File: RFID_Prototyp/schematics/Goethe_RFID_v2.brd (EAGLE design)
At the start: 57.1 x 53.3 mm, 61 parts, among them IC2 LM2937, M1 ARDUINO_R3_SMALL, Q1 IRF8313P, Q2 IRF8313P, Q3 IRF8313P, X1 12V supply

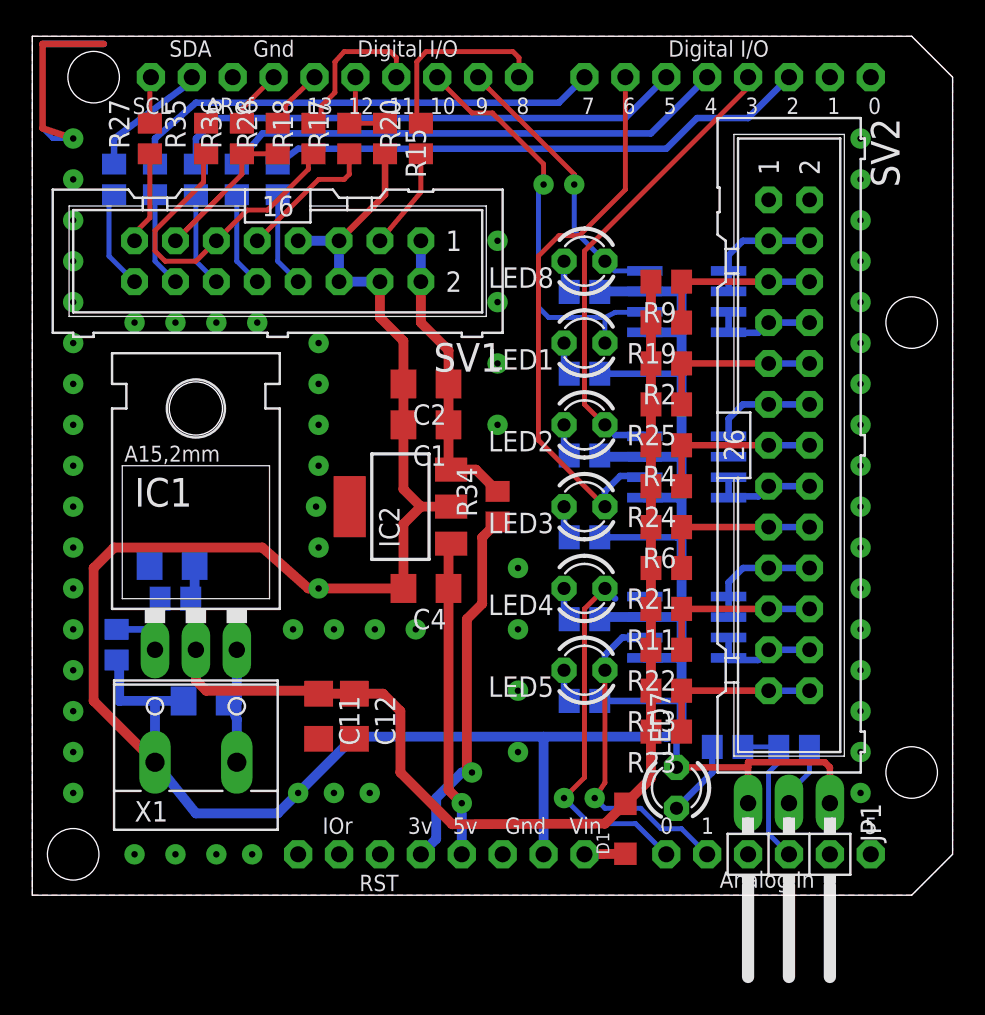
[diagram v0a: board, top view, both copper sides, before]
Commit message: Add RFID lib to repo; Adjust LED regulator voltage; Split RFID firmware in fron/back versions
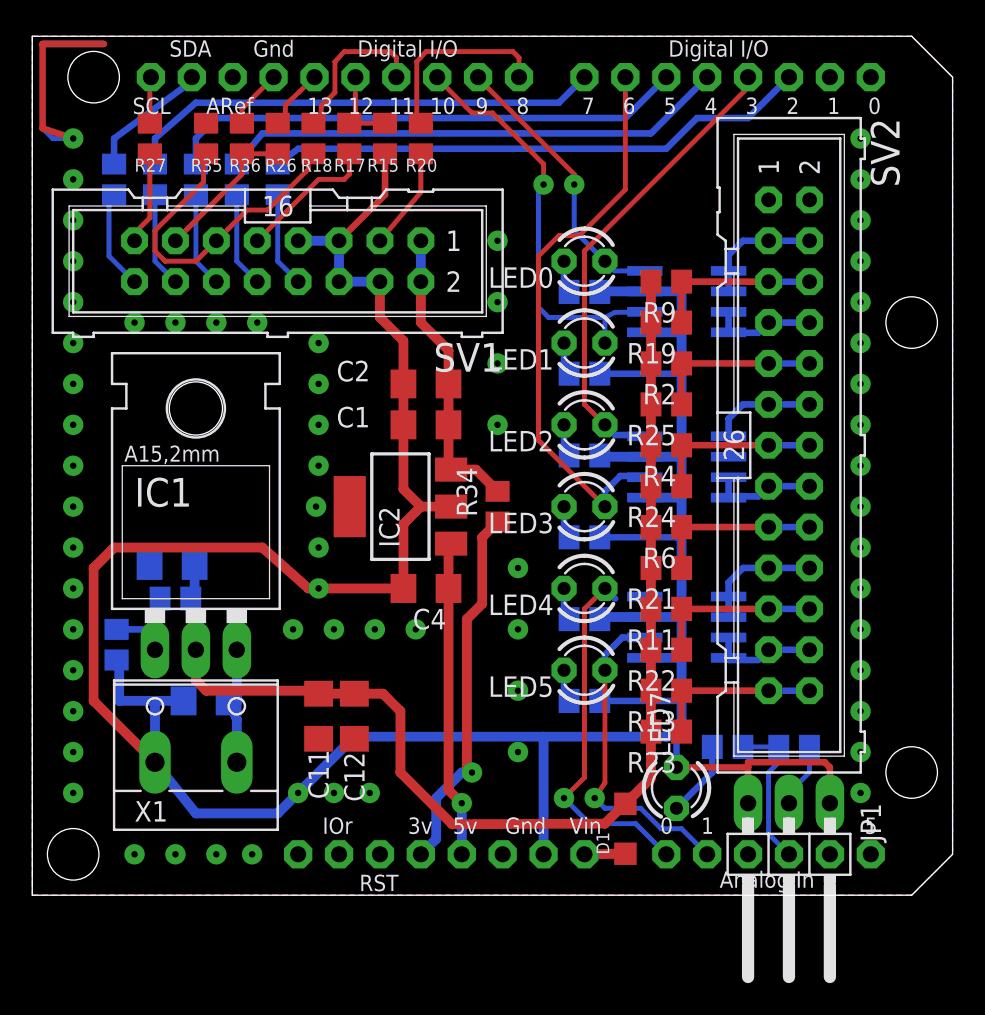
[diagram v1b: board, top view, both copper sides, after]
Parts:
- IC1: value (none) -> LM1086-ADJ
- R16: value 100 -> 132 (220||330)
- R28: value 860 -> 1k1 (2k2||2k2)
- renumbered LED8 to LED0
